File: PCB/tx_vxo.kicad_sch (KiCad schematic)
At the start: 94 parts, among them J1 Key, J3 BNC, J4 2.1 mm Barrel Jack, Q1 2N4401, Q7 2N4403, Q9 2N7000, T5 FT37-43 10T Bifilar, X5 3.582 MHz

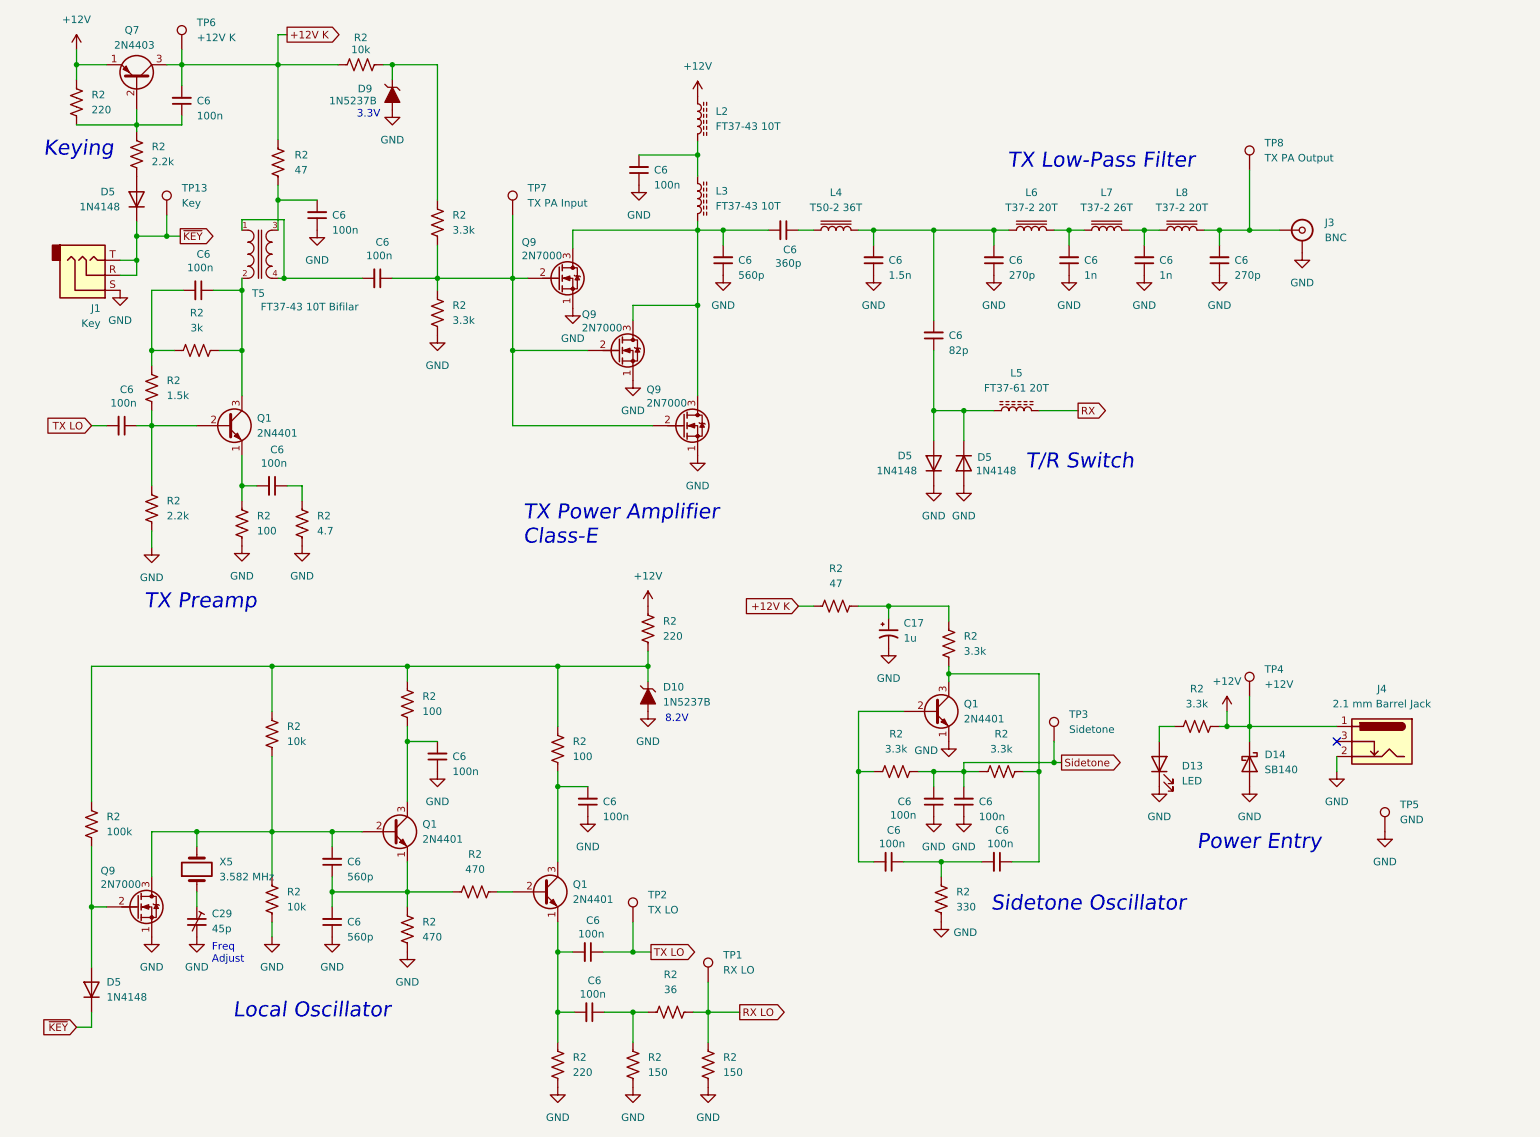
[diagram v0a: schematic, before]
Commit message: Add basic build instructions
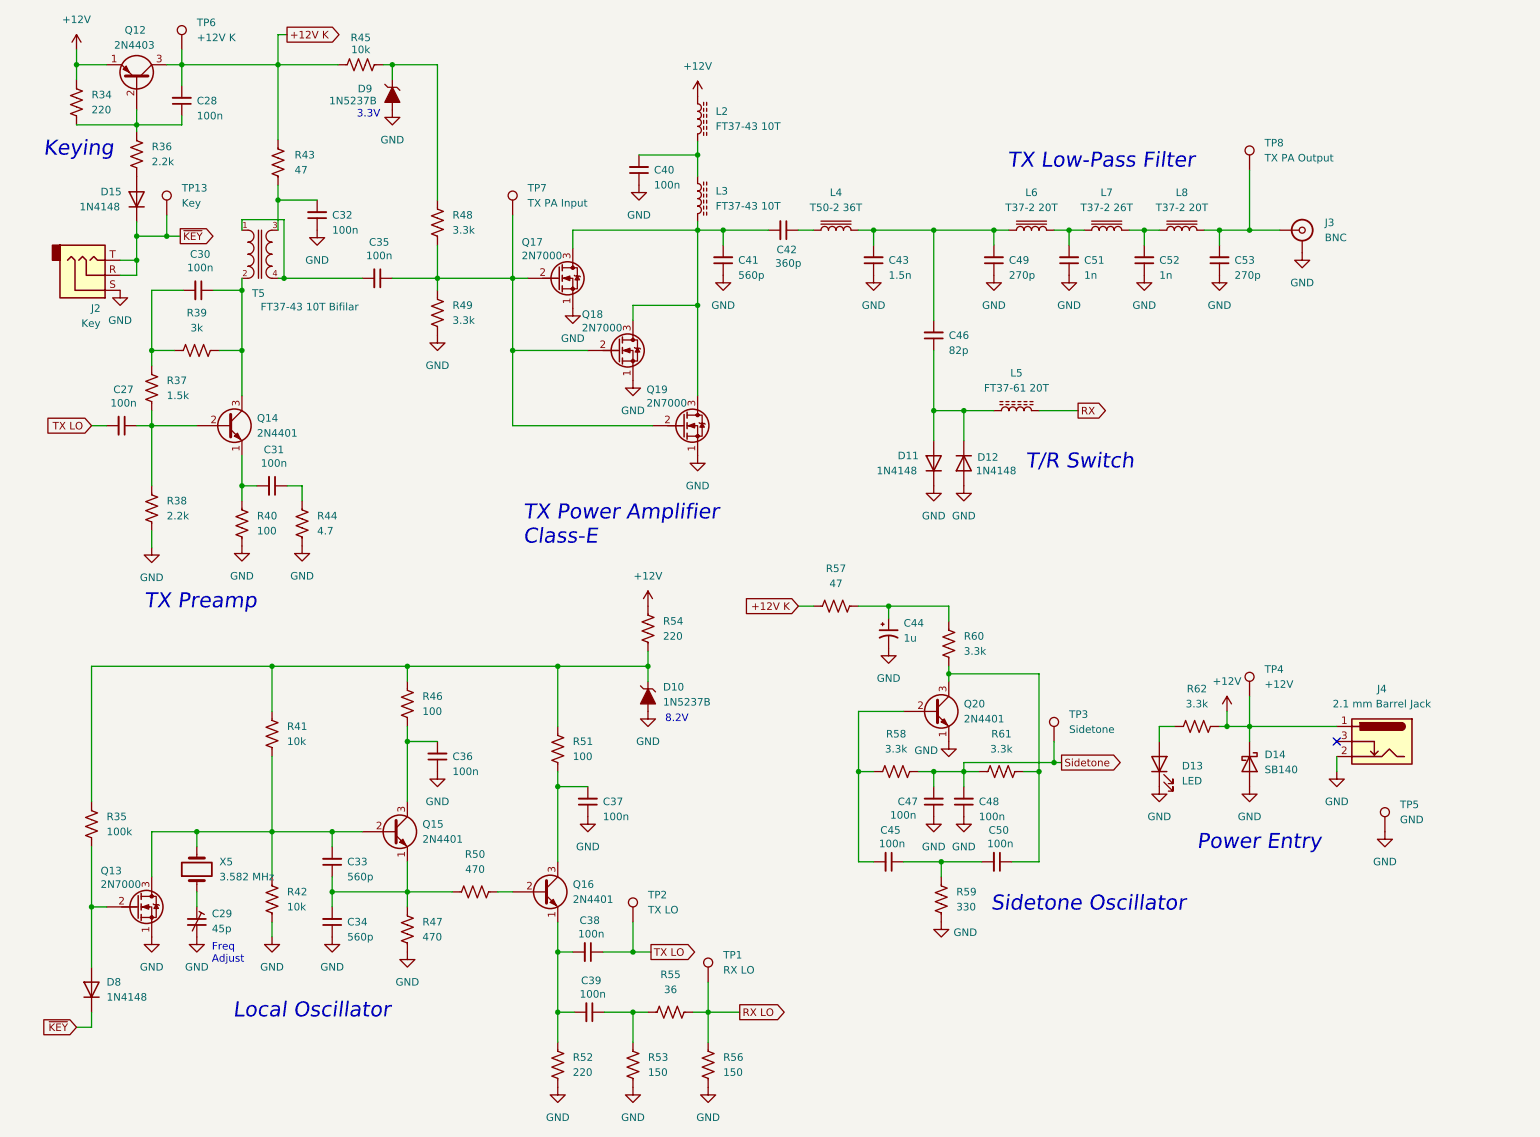
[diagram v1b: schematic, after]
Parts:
- renumbered C6 to C27, C6 to C28, C6 to C30, C6 to C31, C6 to C32, C6 to C33, C6 to C34, C6 to C35, C6 to C36, C6 to C37, C6 to C38, C6 to C39, C6 to C40, C6 to C41, C6 to C42, C6 to C43, C17 to C44, C6 to C45, C6 to C46, C6 to C47, C6 to C48, C6 to C49, C6 to C50, C6 to C51, C6 to C52, C6 to C53, D5 to D11, D5 to D12, D5 to D15, D5 to D8, J1 to J2, Q7 to Q12, Q9 to Q13, Q1 to Q14, Q1 to Q15, Q1 to Q16, Q9 to Q17, Q9 to Q18, Q9 to Q19, Q1 to Q20, R2 to R34, R2 to R35, R2 to R36, R2 to R37, R2 to R38, R2 to R39, R2 to R40, R2 to R41, R2 to R42, R2 to R43, R2 to R44, R2 to R45, R2 to R46, R2 to R47, R2 to R48, R2 to R49, R2 to R50, R2 to R51, R2 to R52, R2 to R53, R2 to R54, R2 to R55, R2 to R56, R2 to R57, R2 to R58, R2 to R59, R2 to R60, R2 to R61, R2 to R62

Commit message: Party Line 80 PCB Rev B
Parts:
- removed C27: 100n, Capacitor_THT:C_Rect_L7.0mm_W2.5mm_P5.00mm, symbol Device:C_Small
- removed D10: 1N5237B, Diode_THT:D_DO-35_SOD27_P7.62mm_Horizontal, symbol EtherkitKicadLibrary:ZENER
- added C28: 1u, Capacitor_THT:CP_Radial_D5.0mm_P2.50mm, symbol Device:C_Polarized_Small_US
- added D15: 1N5237B, EtherkitKicadLibrary:D_DO-35_SOD27_P7.62mm_Horizontal, symbol EtherkitKicadLibrary:ZENER
- added L2: T37-2 22T, EtherkitKicadLibrary:T37-V, symbol Device:L_Iron
- added R62: 1k, Resistor_THT:R_Axial_DIN0207_L6.3mm_D2.5mm_P2.54mm_Vertical, symbol Device:R_US
- added TP14: +3.3V, TestPoint:TestPoint_THTPad_D2.0mm_Drill1.0mm, symbol Connector:TestPoint
- D10: renamed from D9; footprint Diode_THT:D_DO-35_SOD27_P7.62mm_Horizontal -> EtherkitKicadLibrary:D_DO-35_SOD27_P7.62mm_Horizontal
- renumbered C28 to C29, C29 to C30, C30 to C31, C31 to C32, C32 to C33, C33 to C34, C34 to C35, C35 to C36, C36 to C37, C37 to C38, C38 to C39, C39 to C40, C40 to C41, C41 to C42, C42 to C43, C43 to C44, C44 to C45, C45 to C46, C46 to C47, C47 to C48, C48 to C49, C49 to C50, C50 to C51, C51 to C52, C52 to C53, C53 to C54, D15 to D9, L2 to L3, L3 to L4, L4 to L5, L5 to L6, L6 to L7, L7 to L8, L8 to L9, R34 to R33, R35 to R34, R36 to R35, R37 to R36, R38 to R37, R39 to R38, R40 to R39, R41 to R40, R42 to R41, R43 to R42, R44 to R43, R45 to R44, R46 to R45, R47 to R46, R48 to R47, R49 to R48, R50 to R49, R54 to R50, R55 to R54, R56 to R55, R57 to R56, R58 to R57, R59 to R58, R60 to R59, R61 to R60, R62 to R61, TP3 to TP10, TP8 to TP11, TP4 to TP12, TP5 to TP13, TP13 to TP5, TP2 to TP8, TP1 to TP9
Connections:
- net +12V: now also R62.2
- net GND: now also C28.2, D15.1 (A)
- net TX LO: now also Q14.2 (B), R36.2, R37.1
- net at C30.1: now also L2.1; no longer X5.1
- net at R40.1, R45.1, R50.2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: no longer R34.1
- net at D8.2 (A), Q13.2 (G), R34.2: now also C28.1
- net at C34.2, Q15.2 (B), R40.2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: no longer Q13.3 (D)
- new net: L2.2, Q13.3 (D), X5.1
- new net +3.3V: D15.2 (K), R34.1, R62.1, TP14.1
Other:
- note removed: "8.2V"
- moved on the sheet: C30, D8, J4, Q13, R34, R50, TP13
